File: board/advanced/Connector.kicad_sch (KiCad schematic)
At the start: 13 parts, among them J13 UltraSonic, J14 Debug, J15 Display, J16 TouchDisplay, J17 I/O Pins

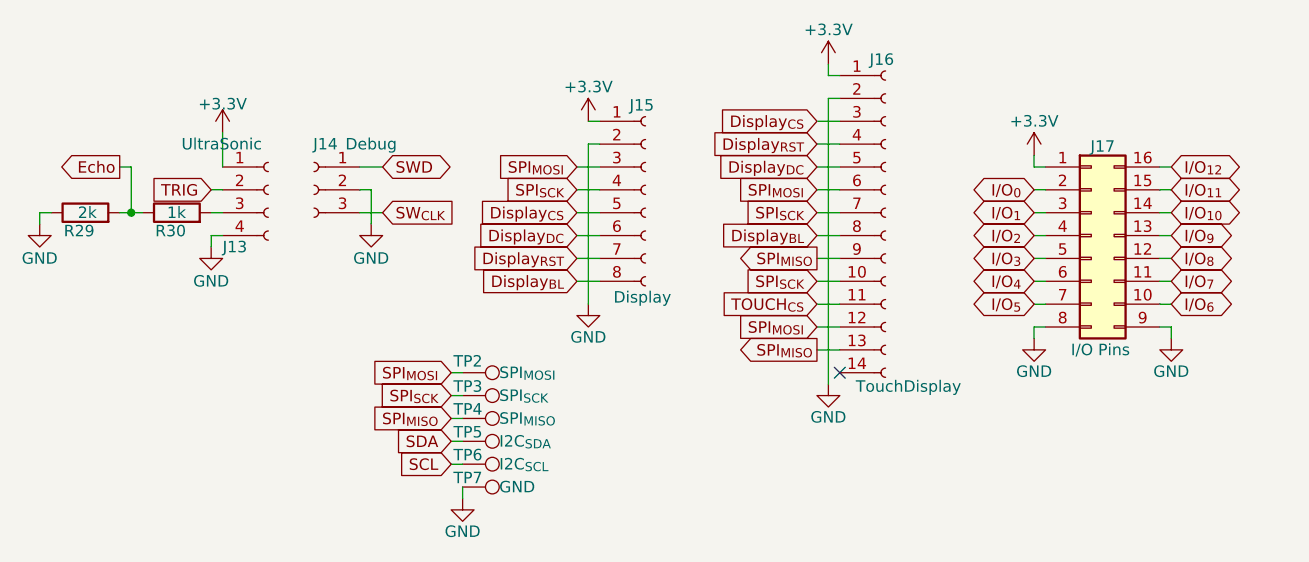
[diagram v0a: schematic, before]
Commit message: put footprints and change schematics
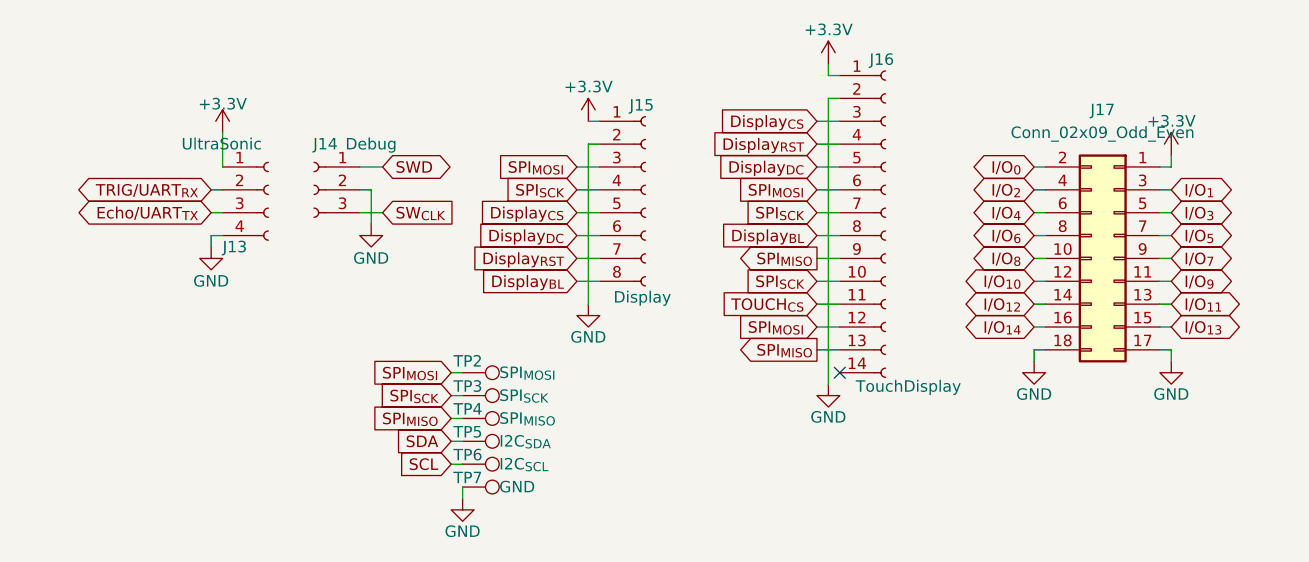
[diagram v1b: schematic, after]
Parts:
- removed J17: I/O Pins, Connector_PinSocket_2.54mm:PinSocket_2x08_P2.54mm_Vertical, symbol Connector_Generic:Conn_02x08_Counter_Clockwise
- removed R29: 2k, Resistor_SMD:R_0603_1608Metric, symbol Device:R
- removed R30: 1k, Resistor_SMD:R_0603_1608Metric, symbol Device:R
- added J17: Conn_02x09_Odd_Even, Connector_PinHeader_2.54mm:PinHeader_2x09_P2.54mm_Vertical, symbol Connector_Generic:Conn_02x09_Odd_Even
- J14: footprint Connector_JST:JST_PH_B3B-PH-SM4-TB_1x03-1MP_P2.00mm_Vertical -> Connector_PinHeader_2.54mm:PinHeader_1x03_P2.54mm_Vertical
- TP2, TP3, TP4, TP5, TP6, TP7: footprint TestPoint:TestPoint_Loop_D2.50mm_Drill1.85mm -> TestPoint:TestPoint_THTPad_2.0x2.0mm_Drill1.0mm
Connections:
- net +3.3V: now also J17.1 (Pin_1)
- net GND: now also J17.17 (Pin_17), J17.18 (Pin_18)
- net I/O_{0}: now also J17.2 (Pin_2)
- net I/O_{10}: now also J17.12 (Pin_12)
- net I/O_{11}: now also J17.13 (Pin_13)
- net I/O_{12}: now also J17.14 (Pin_14)
- net I/O_{1}: now also J17.3 (Pin_3)
- net I/O_{2}: now also J17.4 (Pin_4)
- net I/O_{3}: now also J17.5 (Pin_5)
- net I/O_{4}: now also J17.6 (Pin_6)
- net I/O_{5}: now also J17.7 (Pin_7)
- net I/O_{6}: now also J17.8 (Pin_8)
- net I/O_{7}: now also J17.9 (Pin_9)
- net I/O_{8}: now also J17.10 (Pin_10)
- net I/O_{9}: now also J17.11 (Pin_11)
- net Echo/UART_{TX}: now reaches J13.3 (Pin_3)
- net TRIG renamed TRIG/UART_{RX}
- new net I/O_{13}: J17.15 (Pin_15)
- new net I/O_{14}: J17.16 (Pin_16)

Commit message: change schematics and complete wiring
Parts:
- J17: footprint Connector_PinHeader_2.54mm:PinHeader_2x09_P2.54mm_Vertical -> Connector_PinSocket_2.54mm:PinSocket_2x09_P2.54mm_Vertical
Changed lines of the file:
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@@
 		(on_board yes)
 		(dnp no)
-		(property "Reference" "#PWR073"
+		(property "Reference" "#PWR068"
 			(at 143.51 107.95 0)
 			(hide yes)
@@
 			(project "TurtlePico-Minimal"
 				(path "/7af2d99d-e350-48e7-86b4-20911ea922f3/42224473-68eb-43d4-97ed-5df85a0a50dc"
-					(reference "#PWR073")
+					(reference "#PWR068")
 					(unit 1)
 				)
@@
 		(on_board yes)
 		(dnp no)
-		(property "Reference" "#PWR071"
+		(property "Reference" "#PWR066"
 			(at 125.73 110.49 0)
 			(hide yes)
@@
 			(project "TurtlePico-Minimal"
 				(path "/7af2d99d-e350-48e7-86b4-20911ea922f3/42224473-68eb-43d4-97ed-5df85a0a50dc"
-					(reference "#PWR071")
+					(reference "#PWR066")
 					(unit 1)
 				)
@@
 			)
 		)
-		(property "Footprint" "Connector_PinHeader_2.54mm:PinHeader_2x09_P2.54mm_Vertical"
+		(property "Footprint" "Connector_PinSocket_2.54mm:PinSocket_2x09_P2.54mm_Vertical"
 			(at 226.06 105.41 0)
 			(hide yes)
@@
 		(on_board yes)
 		(dnp no)
-		(property "Reference" "#PWR079"
+		(property "Reference" "#PWR074"
 			(at 217.17 123.19 0)
 			(hide yes)
@@
 			(project "TurtlePico-Minimal"
 				(path "/7af2d99d-e350-48e7-86b4-20911ea922f3/42224473-68eb-43d4-97ed-5df85a0a50dc"
-					(reference "#PWR079")
+					(reference "#PWR074")
 					(unit 1)
 				)
@@
 		(on_board yes)
 		(dnp no)
-		(property "Reference" "#PWR078"
+		(property "Reference" "#PWR073"
 			(at 194.31 125.73 0)
 			(hide yes)
@@
 			(project "TurtlePico-Minimal"
 				(path "/7af2d99d-e350-48e7-86b4-20911ea922f3/42224473-68eb-43d4-97ed-5df85a0a50dc"
-					(reference "#PWR078")
+					(reference "#PWR073")
 					(unit 1)
 				)
@@
 		(on_board yes)
 		(dnp no)
-		(property "Reference" "#PWR081"
+		(property "Reference" "#PWR076"
 			(at 232.41 123.19 0)
 			(hide yes)
@@
 			(project "TurtlePico-Minimal"
 				(path "/7af2d99d-e350-48e7-86b4-20911ea922f3/42224473-68eb-43d4-97ed-5df85a0a50dc"
-					(reference "#PWR081")
+					(reference "#PWR076")
 					(unit 1)
 				)
@@
 		(on_board yes)
 		(dnp no)
-		(property "Reference" "#PWR080"
+		(property "Reference" "#PWR075"
 			(at 232.41 97.79 0)
 			(hide yes)
@@
 			(project "TurtlePico-Minimal"
 				(path "/7af2d99d-e350-48e7-86b4-20911ea922f3/42224473-68eb-43d4-97ed-5df85a0a50dc"
-					(reference "#PWR080")
+					(reference "#PWR075")
 					(unit 1)
 				)
@@
 		(on_board yes)
 		(dnp no)
-		(property "Reference" "#PWR075"
+		(property "Reference" "#PWR070"
 			(at 167.64 93.98 0)
 			(hide yes)
@@
 			(project "TurtlePico-Minimal"
 				(path "/7af2d99d-e350-48e7-86b4-20911ea922f3/42224473-68eb-43d4-97ed-5df85a0a50dc"
-					(reference "#PWR075")
+					(reference "#PWR070")
 					(unit 1)
 				)
@@
 		(on_board yes)
 		(dnp no)
-		(property "Reference" "#PWR074"
+		(property "Reference" "#PWR069"
 			(at 153.67 138.43 0)
 			(hide yes)
@@
 			(project "TurtlePico-Minimal"
 				(path "/7af2d99d-e350-48e7-86b4-20911ea922f3/42224473-68eb-43d4-97ed-5df85a0a50dc"
-					(reference "#PWR074")
+					(reference "#PWR069")
 					(unit 1)
 				)
@@
 		(on_board yes)
 		(dnp no)
-		(property "Reference" "#PWR072"
+		(property "Reference" "#PWR067"
 			(at 127 95.25 0)
 			(hide yes)
@@
 			(project "TurtlePico-Minimal"
 				(path "/7af2d99d-e350-48e7-86b4-20911ea922f3/42224473-68eb-43d4-97ed-5df85a0a50dc"
-					(reference "#PWR072")
+					(reference "#PWR067")
 					(unit 1)
 				)
@@
 		(on_board yes)
 		(dnp no)
-		(property "Reference" "#PWR077"
+		(property "Reference" "#PWR072"
 			(at 194.31 87.63 0)
 			(hide yes)
@@
 			(project "TurtlePico-Minimal"
 				(path "/7af2d99d-e350-48e7-86b4-20911ea922f3/42224473-68eb-43d4-97ed-5df85a0a50dc"
-					(reference "#PWR077")
+					(reference "#PWR072")
 					(unit 1)
 				)
@@
 		(on_board yes)
 		(dnp no)
-		(property "Reference" "#PWR076"
+		(property "Reference" "#PWR071"
 			(at 167.64 116.84 0)
 			(hide yes)
@@
 			(project "TurtlePico-Minimal"
 				(path "/7af2d99d-e350-48e7-86b4-20911ea922f3/42224473-68eb-43d4-97ed-5df85a0a50dc"
-					(reference "#PWR076")
-					(unit 1)
-				)
+					(reference "#PWR071")
+					(unit 1)
+				)
